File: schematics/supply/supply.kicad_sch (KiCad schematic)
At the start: 29 parts, among them J1 power +5V connector from boar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, J2 VSYS connector from Board#1, J21 RFShield_OnePiece, J22 RFShield_OnePiece, J3 RFShield_OnePiece, Q1 IRLML0030, U1 ISO1540, U2 6N137, U3 FAN3100

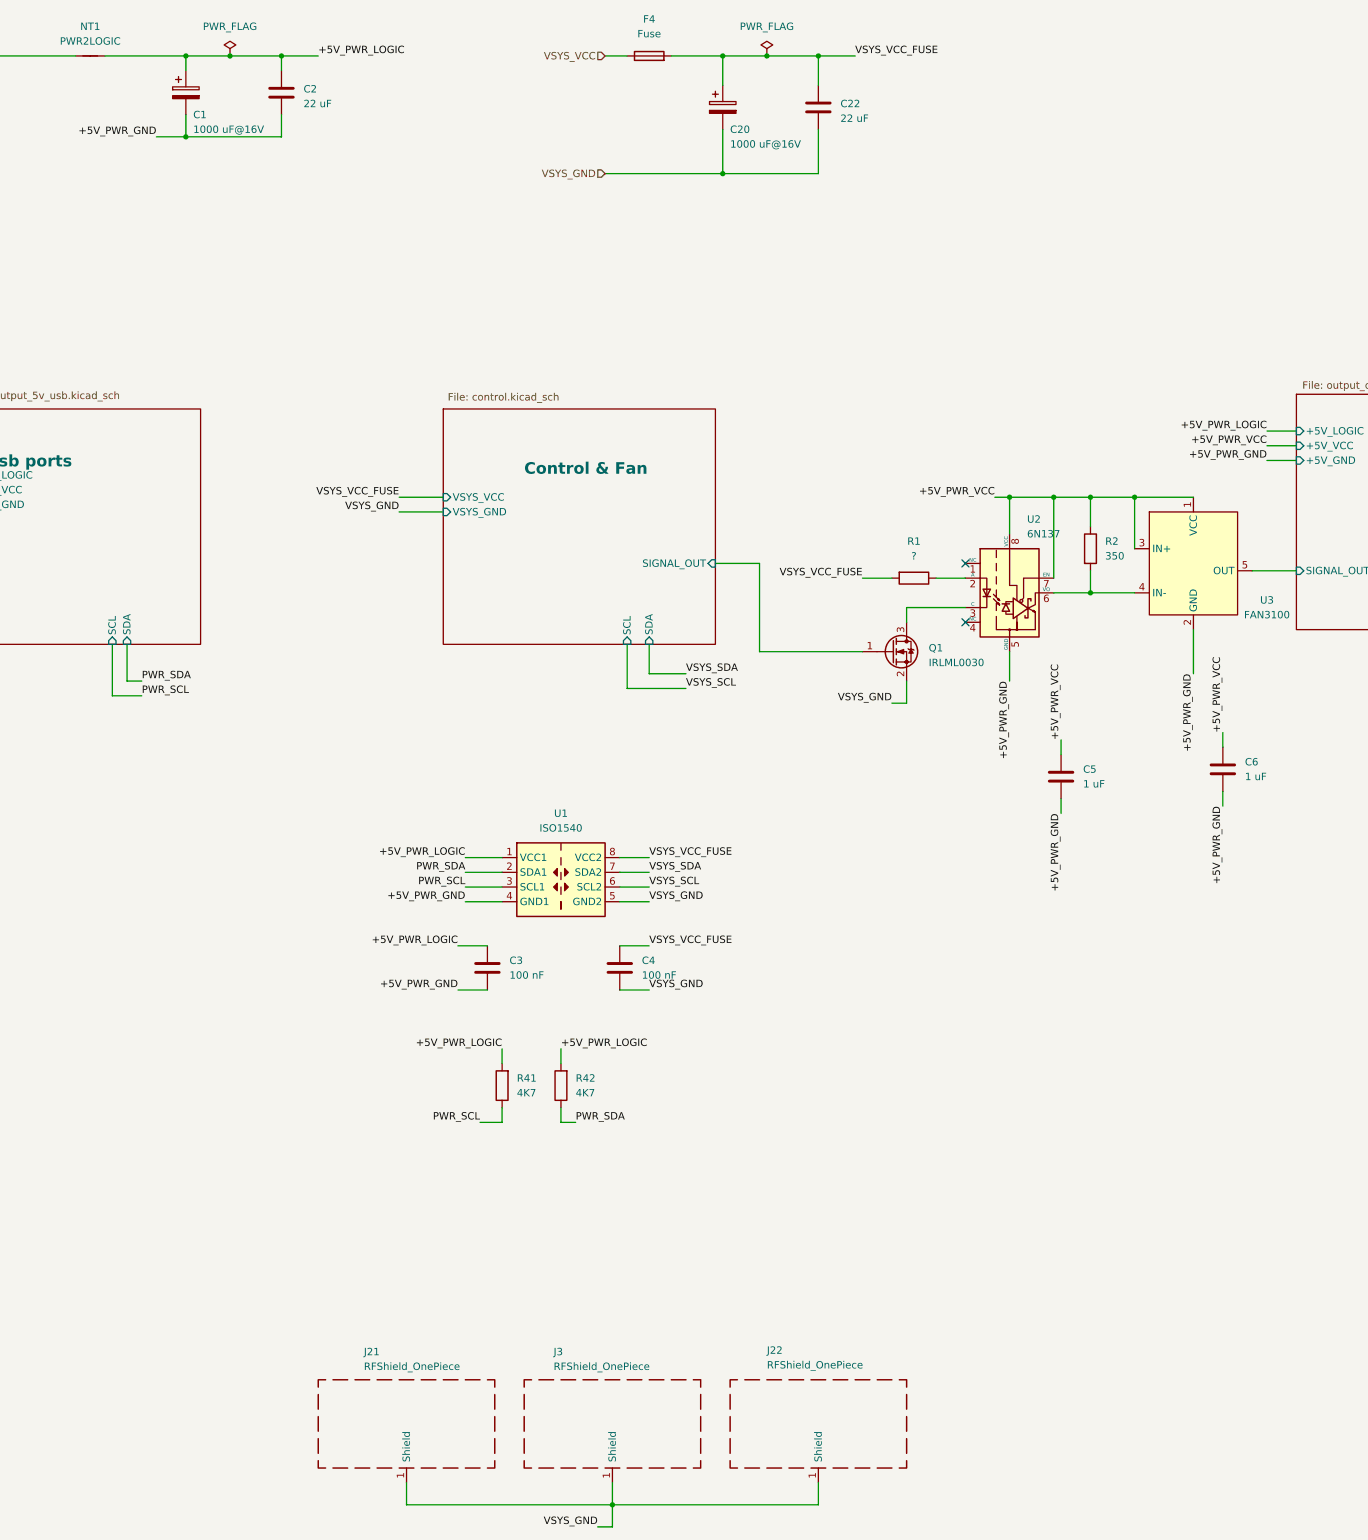
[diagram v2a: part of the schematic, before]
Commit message: some changes in board routing
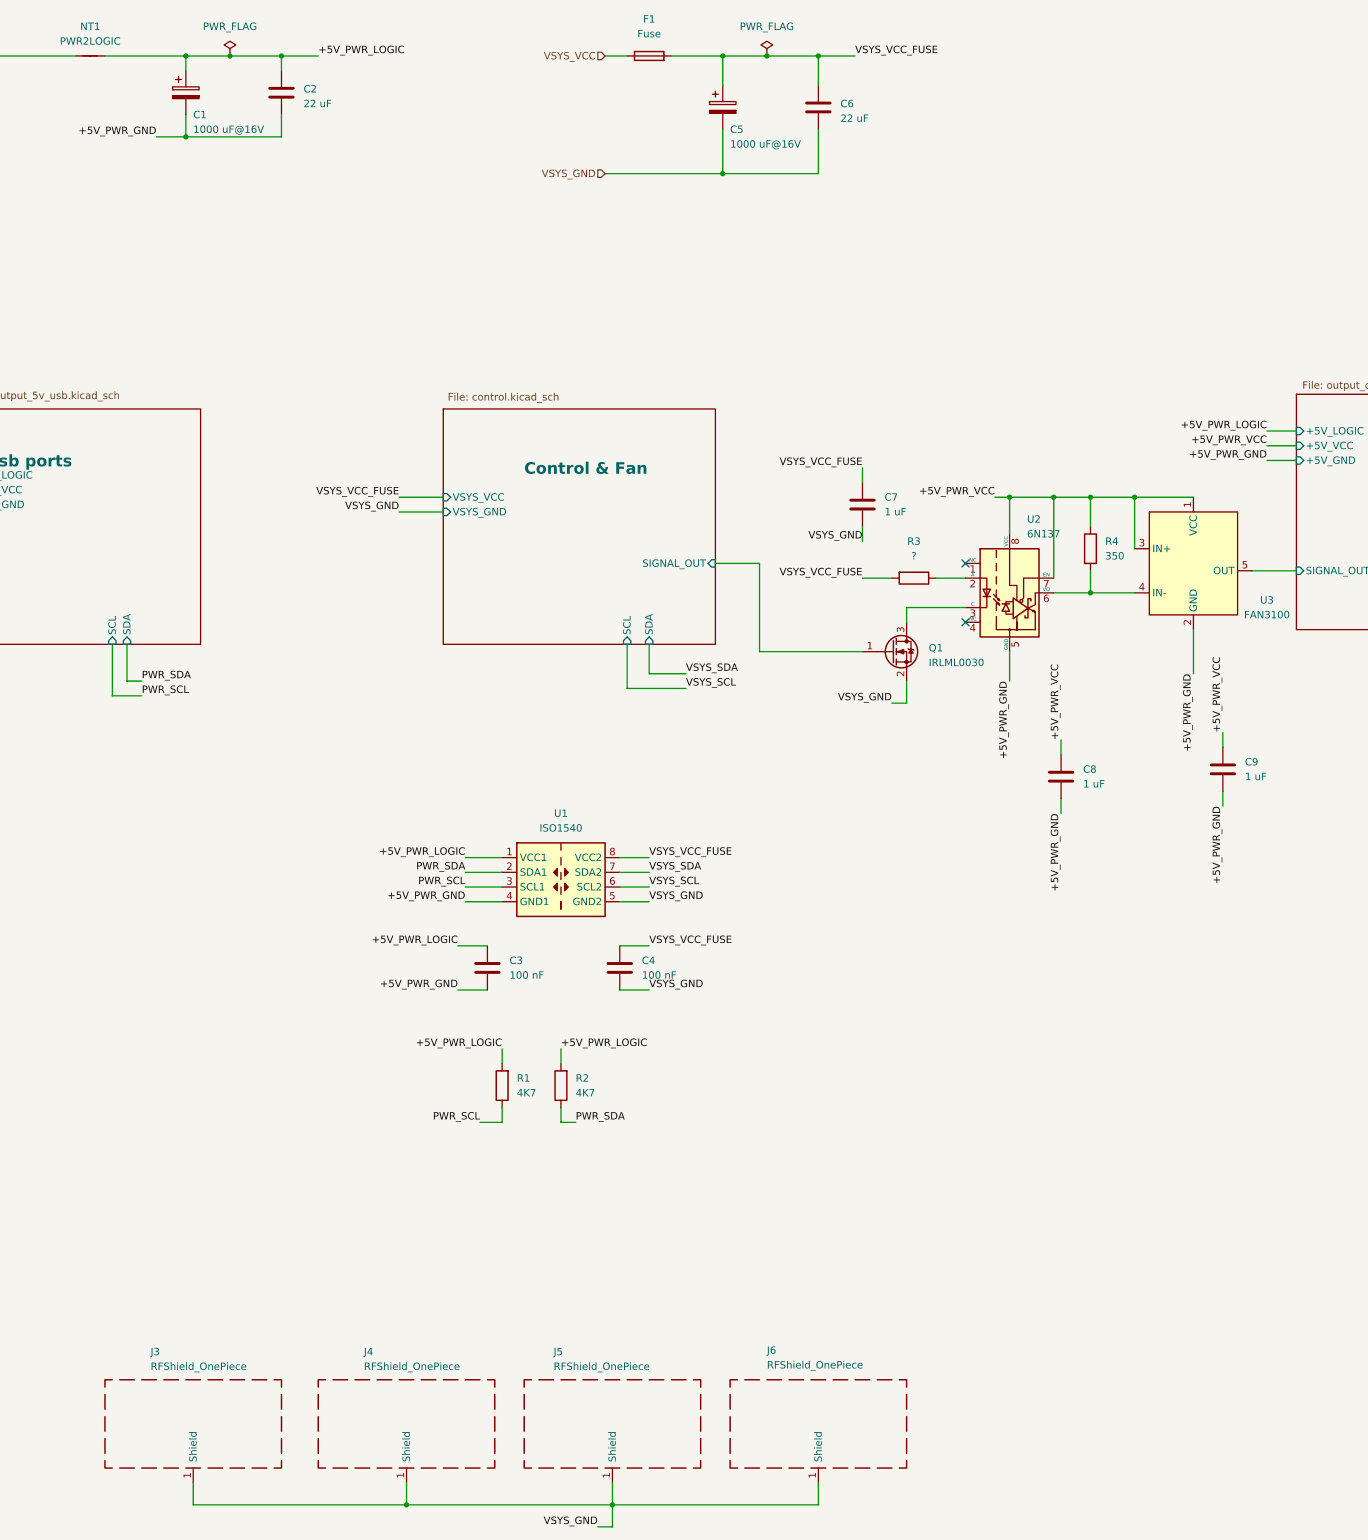
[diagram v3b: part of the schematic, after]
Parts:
- added C7: 1 uF, Capacitor_SMD:C_0603_1608Metric, symbol Device:C
- added J3: RFShield_OnePiece, Library:EMI_SHIELD_1P_2H, symbol Device:RFShield_OnePiece
- renumbered C20 to C5, C22 to C6, C5 to C8, C6 to C9, F4 to F1, J21 to J4, J3 to J5, J22 to J6, R41 to R1, R42 to R2, R1 to R3, R2 to R4
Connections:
- net VSYS_GND: now also C7.2, J3.1 (Shield)
- net VSYS_VCC_FUSE: now also C7.1
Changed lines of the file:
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@@
 	)
 	(junction
+		(at 179.07 273.05)
+		(diameter 0)
+		(color 0 0 0 0)
+	)
+	(junction
 		(at 241.3 22.86)
 		(diameter 0)
@@
 	(wire
 		(pts
+			(xy 257.81 104.14) (xy 257.81 106.68)
+		)
+		(stroke
+			(width 0)
+			(type default)
+		)
+	)
+	(wire
+		(pts
 			(xy 205.74 207.01) (xy 208.28 207.01)
 		)
@@
 	(wire
 		(pts
+			(xy 142.24 273.05) (xy 179.07 273.05)
+		)
+		(stroke
+			(width 0)
+			(type default)
+		)
+	)
+	(wire
+		(pts
 			(xy 241.3 22.86) (xy 233.68 22.86)
 		)
@@
 	(wire
 		(pts
+			(xy 142.24 269.24) (xy 142.24 273.05)
+		)
+		(stroke
+			(width 0)
+			(type default)
+		)
+	)
+	(wire
+		(pts
 			(xy 187.96 176.53) (xy 193.04 176.53)
 		)
@@
 	(wire
 		(pts
+			(xy 257.81 93.98) (xy 257.81 96.52)
+		)
+		(stroke
+			(width 0)
+			(type default)
+		)
+	)
+	(wire
+		(pts
 			(xy 189.23 166.37) (xy 195.58 166.37)
 		)
@@
 		)
 	)
+	(label "VSYS_GND"
+		(at 257.81 106.68 180)
+		(fields_autoplaced yes)
+		(effects
+			(font
+				(size 1.27 1.27)
+			)
+			(justify right bottom)
+		)
+	)
 	(label "+5V_PWR_LOGIC"
 		(at 187.96 176.53 180)
@@
 		)
 	)
+	(label "VSYS_VCC_FUSE"
+		(at 257.81 93.98 180)
+		(fields_autoplaced yes)
+		(effects
+			(font
+				(size 1.27 1.27)
+			)
+			(justify right bottom)
+		)
+	)
 	(label "VSYS_SCL"
 		(at 227.33 132.08 0)
@@
 		(dnp no)
 		(fields_autoplaced yes)
-		(property "Reference" "R42"
+		(property "Reference" "R2"
 			(at 208.28 199.39 0)
 			(effects
@@
 			(project "supply"
 				(path "/1e139717-fcd1-4008-a6ea-4c993845e928"
-					(reference "R42")
+					(reference "R2")
 					(unit 1)
 				)
@@
 		(dnp no)
 		(fields_autoplaced yes)
-		(property "Reference" "#FLG014"
+		(property "Reference" "#FLG06"
 			(at 241.3 20.955 0)
 			(effects
@@
 			(project "supply"
 				(path "/1e139717-fcd1-4008-a6ea-4c993845e928"
-					(reference "#FLG014")
+					(reference "#FLG06")
 					(unit 1)
 				)
@@
 		(on_board yes)
 		(dnp no)
-		(property "Reference" "J22"
+		(property "Reference" "J6"
 			(at 241.3 246.38 0)
 			(effects
@@
 			(project "supply"
 				(path "/1e139717-fcd1-4008-a6ea-4c993845e928"
-					(reference "J22")
+					(reference "J6")
 					(unit 1)
 				)
@@
 		(dnp no)
 		(fields_autoplaced yes)
-		(property "Reference" "F4"
+		(property "Reference" "F1"
 			(at 220.98 16.51 90)
 			(effects
@@
 			(project "supply"
 				(path "/1e139717-fcd1-4008-a6ea-4c993845e928"
-					(reference "F4")
+					(reference "F1")
 					(unit 1)
 				)
@@
 		(dnp no)
 		(fields_autoplaced yes)
-		(property "Reference" "C22"
+		(property "Reference" "C6"
 			(at 254 31.115 0)
 			(effects
@@
 			(project "supply"
 				(path "/1e139717-fcd1-4008-a6ea-4c993845e928"
-					(reference "C22")
+					(reference "C6")
 					(unit 1)
 				)
@@
 		(dnp no)
 		(fields_autoplaced yes)
-		(property "Reference" "R41"
+		(property "Reference" "R1"
 			(at 198.12 199.39 0)
 			(effects
@@
 			(project "supply"
 				(path "/1e139717-fcd1-4008-a6ea-4c993845e928"
-					(reference "R41")
+					(reference "R1")
 					(unit 1)
 				)
@@
 		(on_board yes)
 		(dnp no)
-		(property "Reference" "J3"
+		(property "Reference" "J5"
 			(at 204.47 246.634 0)
 			(effects
@@
 			(project "supply"
 				(path "/1e139717-fcd1-4008-a6ea-4c993845e928"
-					(reference "J3")
+					(reference "J5")
 					(unit 1)
 				)
@@
 		(on_board yes)
 		(dnp no)
-		(property "Reference" "J21"
+		(property "Reference" "J4"
 			(at 171.704 246.634 0)
 			(effects
@@
 			(project "supply"
 				(path "/1e139717-fcd1-4008-a6ea-4c993845e928"
-					(reference "J21")
+					(reference "J4")
 					(unit 1)
 				)
@@
 		(dnp no)
 		(fields_autoplaced yes)
-		(property "Reference" "R1"
+		(property "Reference" "R3"
 			(at 266.7 106.68 90)
 			(effects
@@
 			(project "supply"
 				(path "/1e139717-fcd1-4008-a6ea-4c993845e928"
-					(reference "R1")
+					(reference "R3")
 					(unit 1)
 				)
@@
 	)
 	(symbol
+		(lib_id "Device:C")
+		(at 257.81 100.33 0)
+		(unit 1)
+		(exclude_from_sim no)
+		(in_bom yes)
+		(on_board yes)
+		(dnp no)
+		(fields_autoplaced yes)
+		(property "Reference" "C7"
+			(at 261.62 99.06 0)
+			(effects
+				(font
+					(size 1.27 1.27)
+				)
+				(justify left)
+			)
+		)
+		(property "Value" "1 uF"
+			(at 261.62 101.6 0)
+			(effects
+				(font
+					(size 1.27 1.27)
+				)
+				(justify left)
+			)
+		)
+		(property "Footprint" "Capacitor_SMD:C_0603_1608Metric"
+			(at 258.7752 104.14 0)
+			(effects
+				(font
+					(size 1.27 1.27)
+				)
+				(hide yes)
+			)
+		)
+		(property "Datasheet" "~"
+			(at 257.81 100.33 0)
+			(effects
+				(font
+					(size 1.27 1.27)
+				)
+				(hide yes)
+			)
+		)
+		(property "Description" "Unpolarized capacitor"
+			(at 257.81 100.33 0)
+			(effects
+				(font
+					(size 1.27 1.27)
+				)
+				(hide yes)
+			)
+		)
+		(pin "1"
+		)
+		(pin "2"
+		)
+		(instances
+			(project "supply"
+				(path "/1e139717-fcd1-4008-a6ea-4c993845e928"
+					(reference "C7")
+					(unit 1)
+				)
+			)
+		)
+	)
+	(symbol
 		(lib_id "Mechanical:MountingHole")
 		(at 383.54 214.63 0)
@@
 		(dnp no)
 		(fields_autoplaced yes)
-		(property "Reference" "C5"
+		(property "Reference" "C8"
 			(at 295.91 146.05 0)
 			(effects
@@
 			(project "supply"
 				(path "/1e139717-fcd1-4008-a6ea-4c993845e928"
-					(reference "C5")
+					(reference "C8")
 					(unit 1)
 				)
@@
 		(on_board yes)
 		(dnp no)
-		(property "Reference" "C20"
+		(property "Reference" "C5"
 			(at 234.95 35.56 0)
 			(effects
@@
 			(project "supply"
 				(path "/1e139717-fcd1-4008-a6ea-4c993845e928"
-					(reference "C20")
+					(reference "C5")
+					(unit 1)
+				)
+			)
+		)
+	)
+	(symbol
+		(lib_id "Device:RFShield_OnePiece")
+		(at 142.24 259.08 0)
+		(unit 1)
+		(exclude_from_sim no)
+		(in_bom yes)
+		(on_board yes)
+		(dnp no)
+		(property "Reference" "J3"
+			(at 134.874 246.634 0)
+			(effects
+				(font
+					(size 1.27 1.27)
+				)
+				(justify left)
+			)
+		)
+		(property "Value" "RFShield_OnePiece"
+			(at 134.874 249.174 0)
+			(effects
+				(font
+					(size 1.27 1.27)
+				)
+				(justify left)
+			)
+		)
+		(property "Footprint" "Library:EMI_SHIELD_1P_2H"
+			(at 142.24 261.62 0)
+			(effects
+				(font
+					(size 1.27 1.27)
+				)
+				(hide yes)
+			)
+		)
+		(property "Datasheet" "~"
+			(at 142.24 261.62 0)
+			(effects
+				(font
+					(size 1.27 1.27)
+				)
+				(hide yes)
+			)
+		)
+		(property "Description" "One-piece EMI RF shielding cabinet"
+			(at 142.24 259.08 0)
+			(effects
+				(font
+					(size 1.27 1.27)
+				)
+				(hide yes)
+			)
+		)
+		(pin "1"
+		)
+		(instances
+			(project "supply"
+				(path "/1e139717-fcd1-4008-a6ea-4c993845e928"
+					(reference "J3")
 					(unit 1)
 				)
@@
 		(dnp no)
 		(fields_autoplaced yes)
-		(property "Reference" "C6"
+		(property "Reference" "C9"
 			(at 323.85 144.78 0)
 			(effects
@@
 			(project "supply"
 				(path "/1e139717-fcd1-4008-a6ea-4c993845e928"
-					(reference "C6")
+					(reference "C9")
 					(unit 1)
 				)
@@
 		(dnp no)
 		(fields_autoplaced yes)
-		(property "Reference" "R2"
+		(property "Reference" "R4"
 			(at 299.72 106.6799 0)
 			(effects
@@
 			(project "supply"
 				(path "/1e139717-fcd1-4008-a6ea-4c993845e928"
-					(reference "R2")
+					(reference "R4")
 					(unit 1)
 				)

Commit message: Boards prepared to order
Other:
- moved on the sheet: J1, J2
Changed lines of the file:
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@@
 	(wire
 		(pts
-			(xy 66.04 38.1) (xy 62.23 38.1)
+			(xy 66.04 30.48) (xy 62.23 30.48)
 		)
 		(stroke
@@
 	(wire
 		(pts
-			(xy 66.04 17.78) (xy 62.23 17.78)
+			(xy 66.04 20.32) (xy 62.23 20.32)
 		)
 		(stroke
@@
 	(wire
 		(pts
-			(xy 66.04 30.48) (xy 62.23 30.48)
+			(xy 66.04 38.1) (xy 62.23 38.1)
 		)
 		(stroke
@@
 	(wire
 		(pts
-			(xy 66.04 20.32) (xy 62.23 20.32)
+			(xy 66.04 17.78) (xy 62.23 17.78)
 		)
 		(stroke
@@
 	(wire
 		(pts
-			(xy 66.04 35.56) (xy 62.23 35.56)
+			(xy 66.04 33.02) (xy 62.23 33.02)
 		)
 		(stroke
@@
 	(wire
 		(pts
-			(xy 66.04 33.02) (xy 62.23 33.02)
+			(xy 66.04 35.56) (xy 62.23 35.56)
 		)
 		(stroke
@@
 	)
 	(label "+5V_PWR_VCC"
-		(at 66.04 20.32 0)
+		(at 66.04 17.78 0)
 		(fields_autoplaced yes)
 		(effects
@@
 	)
 	(label "VSYS_SDA"
-		(at 66.04 35.56 0)
+		(at 66.04 33.02 0)
 		(fields_autoplaced yes)
 		(effects
@@
 	)
 	(label "VSYS_SCL"
-		(at 66.04 38.1 0)
+		(at 66.04 30.48 0)
 		(fields_autoplaced yes)
 		(effects
@@
 	)
 	(label "VSYS_VCC"
-		(at 66.04 33.02 0)
+		(at 66.04 35.56 0)
 		(fields_autoplaced yes)
 		(effects
@@
 	)
 	(label "+5V_PWR_GND"
-		(at 66.04 17.78 0)
+		(at 66.04 20.32 0)
 		(fields_autoplaced yes)
 		(effects
@@
 	)
 	(label "VSYS_GND"
-		(at 66.04 30.48 0)
+		(at 66.04 38.1 0)
 		(fields_autoplaced yes)
 		(effects
@@
 	(symbol
 		(lib_id "Connector:Conn_01x02_Socket")
-		(at 57.15 20.32 180)
+		(at 57.15 17.78 0)
+		(mirror y)
 		(unit 1)
 		(exclude_from_sim no)
@@
 		(dnp no)
 		(property "Reference" "J1"
-			(at 52.578 17.526 0)
+			(at 52.578 20.574 0)
 			(effects
 				(font
@@
 		)
 		(property "Value" "power +5V connector from board#1"
-			(at 37.846 20.574 0)
+			(at 37.846 17.526 0)
 			(effects
 				(font
@@
 		)
 		(property "Footprint" "Connector_Wire:SolderWire-1.5sqmm_1x02_P6mm_D1.7mm_OD3mm"
-			(at 57.15 20.32 0)
+			(at 57.15 17.78 0)
 			(effects
 				(font
@@
 		)
 		(property "Datasheet" "~"
-			(at 57.15 20.32 0)
+			(at 57.15 17.78 0)
 			(effects
 				(font
@@
 		)
 		(property "Description" "Generic connector, single row, 01x02, script generated"
-			(at 57.15 20.32 0)
+			(at 57.15 17.78 0)
 			(effects
 				(font
@@
 	(symbol
 		(lib_id "Connector:Conn_01x04_Socket")
-		(at 57.15 35.56 180)
+		(at 57.15 33.02 0)
+		(mirror y)
 		(unit 1)
 		(exclude_from_sim no)
@@
 		(dnp no)
 		(property "Reference" "J2"
-			(at 55.372 30.734 0)
+			(at 55.372 37.846 0)
 			(effects
 				(font
@@
 		)
 		(property "Value" "VSYS connector from Board#1"
-			(at 55.88 33.0201 0)
+			(at 55.88 35.5599 0)
 			(effects
 				(font
@@
 		)
 		(property "Footprint" "Connector_JST:JST_XH_B4B-XH-A_1x04_P2.50mm_Vertical"
-			(at 57.15 35.56 0)
+			(at 57.15 33.02 0)
 			(effects
 				(font
@@
 		)
 		(property "Datasheet" "~"
-			(at 57.15 35.56 0)
+			(at 57.15 33.02 0)
 			(effects
 				(font
@@
 		)
 		(property "Description" "Generic connector, single row, 01x04, script generated"
-			(at 57.15 35.56 0)
+			(at 57.15 33.02 0)
 			(effects
 				(font

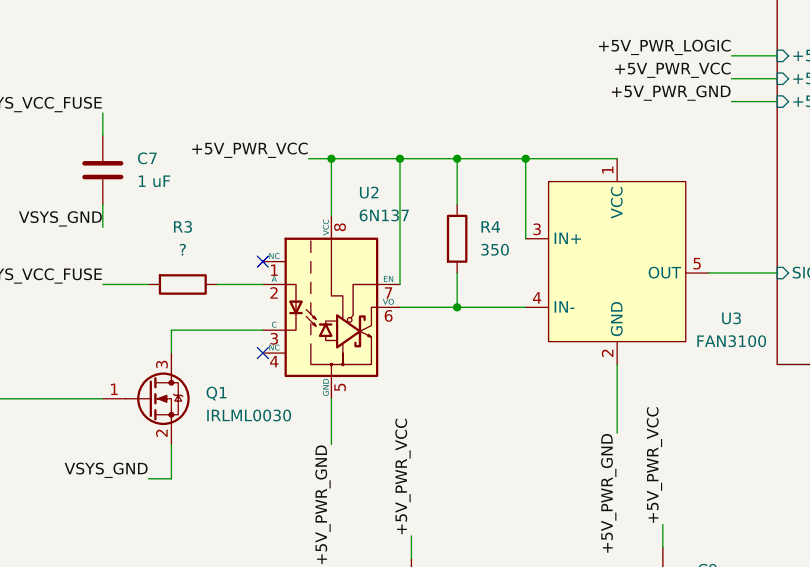
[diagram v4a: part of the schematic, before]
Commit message: power board works (except power output driver, not tested yet), I ready to solder control board
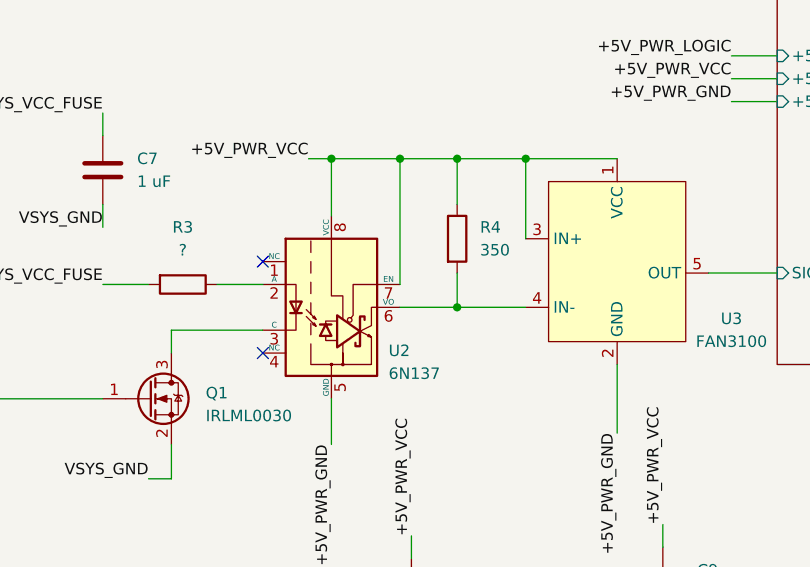
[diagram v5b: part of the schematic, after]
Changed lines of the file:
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@@
 		(on_board yes)
 		(dnp no)
-		(fields_autoplaced yes)
 		(property "Reference" "U2"
-			(at 286.2265 102.87 0)
+			(at 289.56 120.396 0)
 			(effects
 				(font
@@
 		)
 		(property "Value" "6N137"
-			(at 286.2265 105.41 0)
+			(at 289.56 122.936 0)
 			(effects
 				(font
